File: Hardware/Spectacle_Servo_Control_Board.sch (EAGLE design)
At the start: 47 parts, among them J1 FTDI_DEVICE, J10 AUDIO-JACK3, J3 USB-MICROB, J4 AUDIO-JACK3, U1 CY8C4146LQI-S422, U2 3.3V/150mA

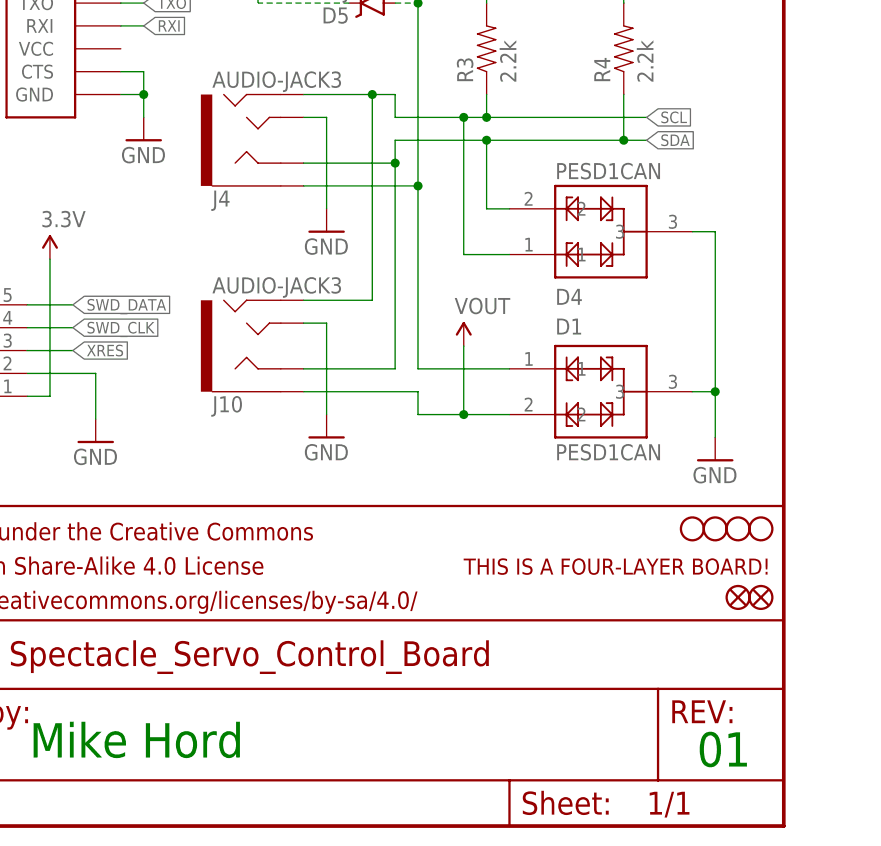
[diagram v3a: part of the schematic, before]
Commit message: Add servo.h, .project, in/out labels
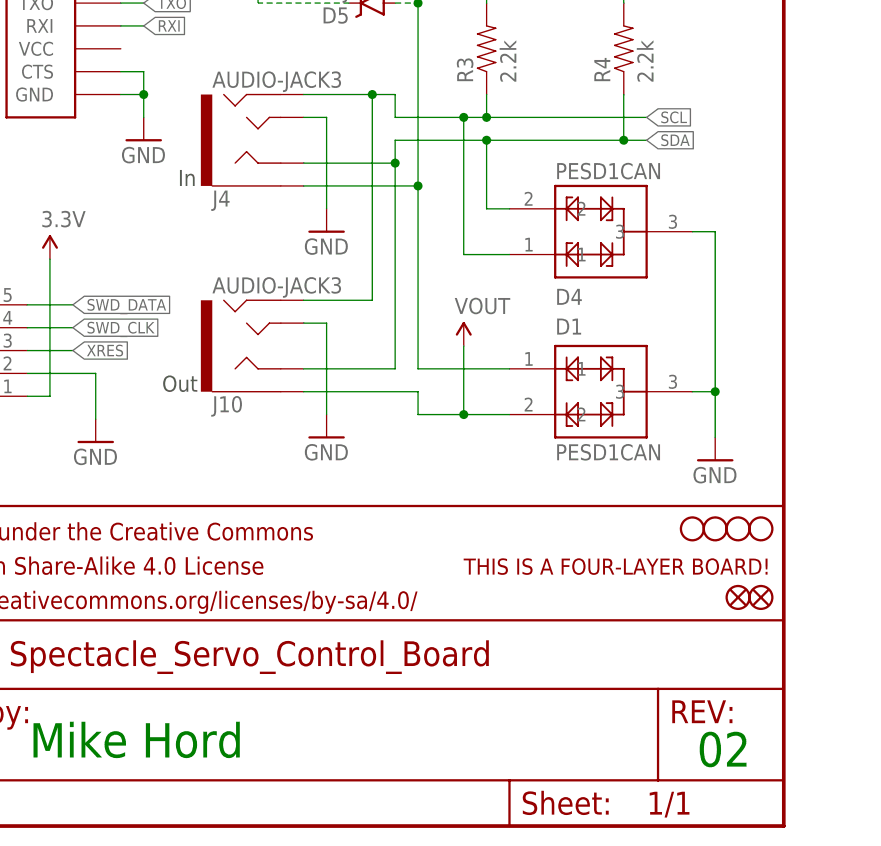
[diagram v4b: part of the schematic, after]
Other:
- note added: "02"
- note added: "In"
- note added: "Out"
- note removed: "01"
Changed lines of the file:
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@@
 <wire x1="66.04" y1="86.36" x2="0" y2="86.36" width="0.3048" layer="97" style="longdash"/>
 <text x="165.1" y="7.62" size="3.81" layer="91" font="vector">Mike Hord</text>
-<text x="239.268" y="6.604" size="3.81" layer="91" font="vector">01</text>
+<text x="239.268" y="6.604" size="3.81" layer="91" font="vector">02</text>
 <wire x1="106.68" y1="114.3" x2="248.92" y2="114.3" width="0.3048" layer="97" style="longdash"/>
 <text x="109.22" y="116.84" size="3.81" layer="97" font="vector">MCU</text>
@@
 <wire x1="106.68" y1="35.56" x2="106.68" y2="22.86" width="0.3048" layer="97" style="longdash"/>
 <wire x1="106.68" y1="22.86" x2="66.04" y2="22.86" width="0.3048" layer="97" style="longdash"/>
+<text x="181.61" y="71.12" size="1.778" layer="97">In</text>
+<text x="179.832" y="48.26" size="1.778" layer="97">Out</text>
 </plain>
 <instances>
